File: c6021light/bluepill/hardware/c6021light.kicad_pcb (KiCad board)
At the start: 2 copper layers, 100 x 50 mm, 80 parts, among them J1 Barrel_Jack_Switch, J10 Conn_01x02, J11 Conn_01x02, J12 XpressNet, J2 Conn_02x04_Odd_Even, J3 Conn_02x16_Row_Letter_First, J30 Loconet, J31 Conn_01x02, J32 Conn_01x02, J4 Conn_01x02, J5 Grove I2C, J50 USB_B_Micro, J51 Conn_01x06, J52 Debug UART, J6 Conn_01x02, J7 Conn_01x02, J8 RJ45, Q30 BC337, Q31 BC547, Q32 BC547, SW1 SW_Push, U1 L7805, U10 SN75176, U2 L7808, U3 MCP2562, U30 LM393, U4 ISO1050DUB, U50 CH340C

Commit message: fix some bugs on PCb
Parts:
- moved C52 2.73 mm to (177.2, 60.9)
- moved D1 2.21 mm to (157.3, 57.0)
- moved J51 1.18 mm to (167.2, 64.1)
- moved C51 1.18 mm to (167.0, 54.9)
- moved U50 1.04 mm to (172.5, 60.6)
- moved C50 0.89 mm to (171.1, 54.0)
- moved R3 0.83 mm to (164.1, 64.2)
- moved R11 0.82 mm to (153.9, 60.8)
- moved R12 0.76 mm to (153.9, 63.8)
- moved J50 0.09 mm to (178.5, 52.8)
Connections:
- J51 pad 6: Net-(J51-Pad6) -> /RTS
- J52 pad 1: /DTR -> /CTS
- J52 pad 5: /CTS -> /RTS
- U50 pad 14: Net-(J51-Pad6) -> /RTS
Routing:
- net /DTR: track 17.7 -> 3.15 mm
- net /RTS: track 0.00 -> 10.4 mm
- net Net-(BP1-Pad25): track 19.1 -> 22.5 mm
- net /CTS: track 17.0 -> 20.0 mm
- net Net-(J51-Pad6): track 3.02 -> 0.00 mm
- net Net-(C52-Pad1): track 5.07 -> 2.33 mm
- net /TxD: track 68.2 -> 66.0 mm
- net Net-(BP1-Pad29): track 16.5 -> 18.3 mm
- net Net-(BP1-Pad30): track 12.8 -> 14.3 mm
- net Net-(D1-Pad2): track 3.13 -> 4.44 mm
- net GND: track 247.7 -> 246.5 mm, vias 24 -> 25
- net Net-(J50-Pad3): track 8.84 -> 9.92 mm, vias 2 -> 0
- net Net-(R12-Pad1): track 39.5 -> 40.6 mm
- net Net-(C50-Pad1): track 13.9 -> 13.3 mm
- net /RxD: track 72.3 -> 72.9 mm

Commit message: remove C32
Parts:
- removed C32: 1n, Capacitor_THT:C_Disc_D3.0mm_W1.6mm_P2.50mm
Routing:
- net Net-(C32-Pad1): track 29.0 -> 6.75 mm

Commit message: save PCB forgotten
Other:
- board text added: "Damian Philipp 2020/12 Gerhard Bertelsmann"
- board text removed: "Damian Philipp 2020/08 Gerhard Bertelsmann"

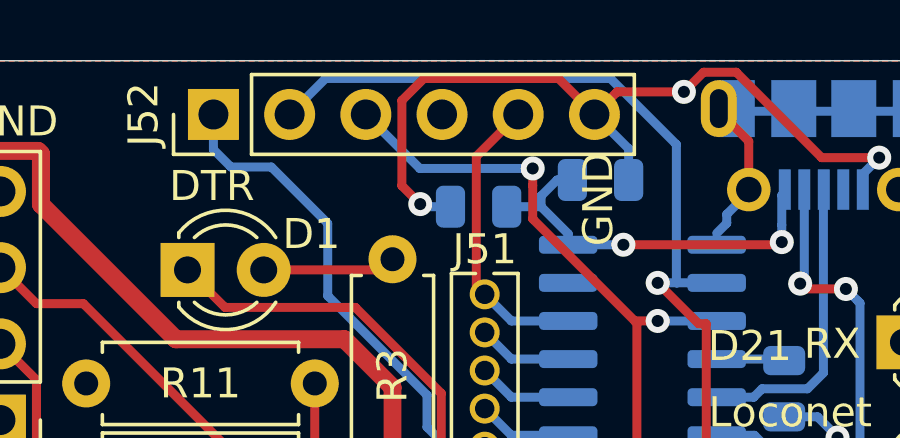
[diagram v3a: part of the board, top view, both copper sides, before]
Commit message: swap TxD and RxD on J52 header for standard USB2Serial Moduls
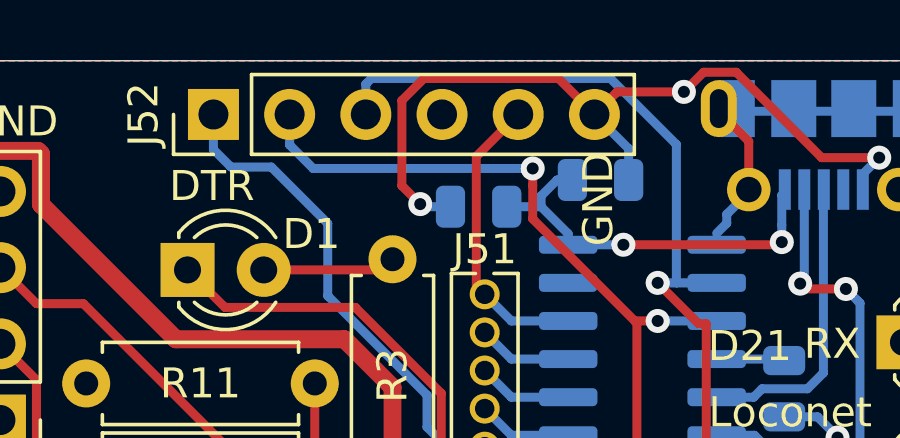
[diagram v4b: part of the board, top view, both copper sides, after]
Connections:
- J52 pad 2: /RxD -> /TxD
- J52 pad 3: /TxD -> /RxD
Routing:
- net /TxD: track 66.0 -> 69.1 mm
- net /RxD: track 72.9 -> 71.0 mm

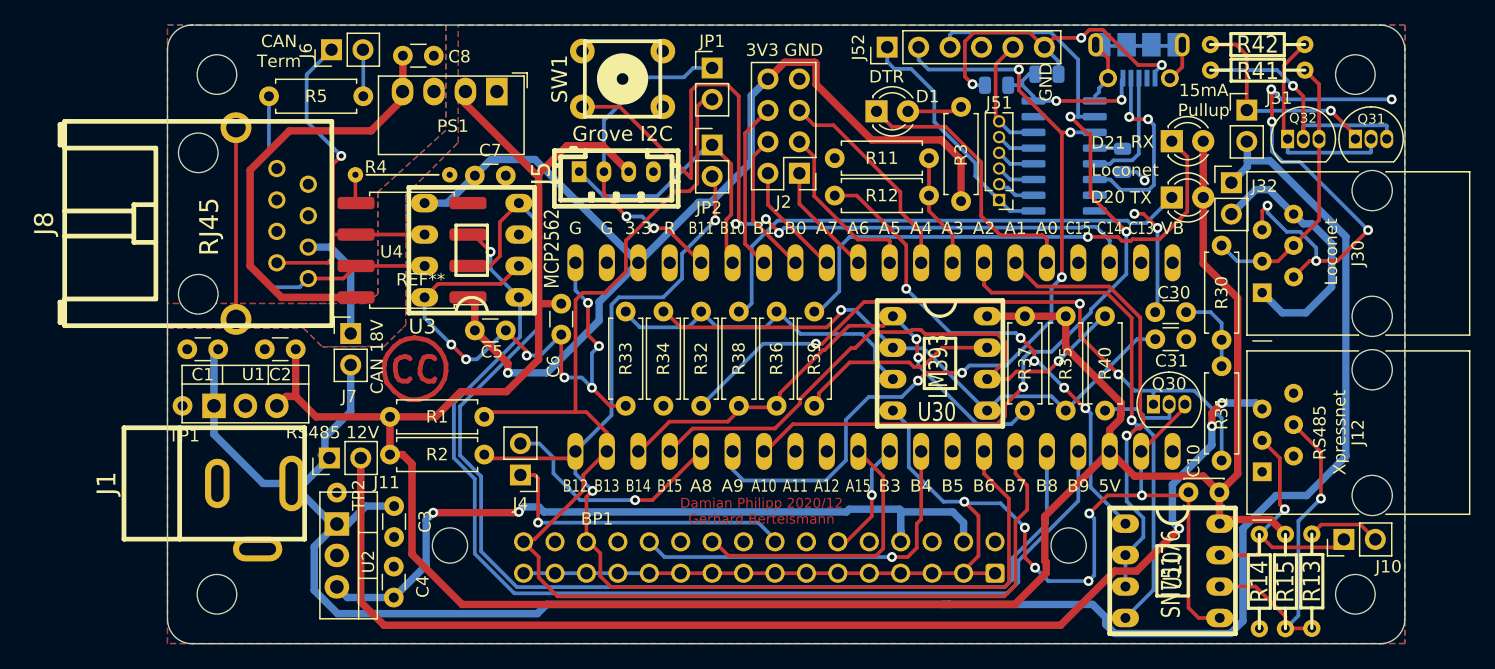
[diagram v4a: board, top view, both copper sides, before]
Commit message: fix silkscreen
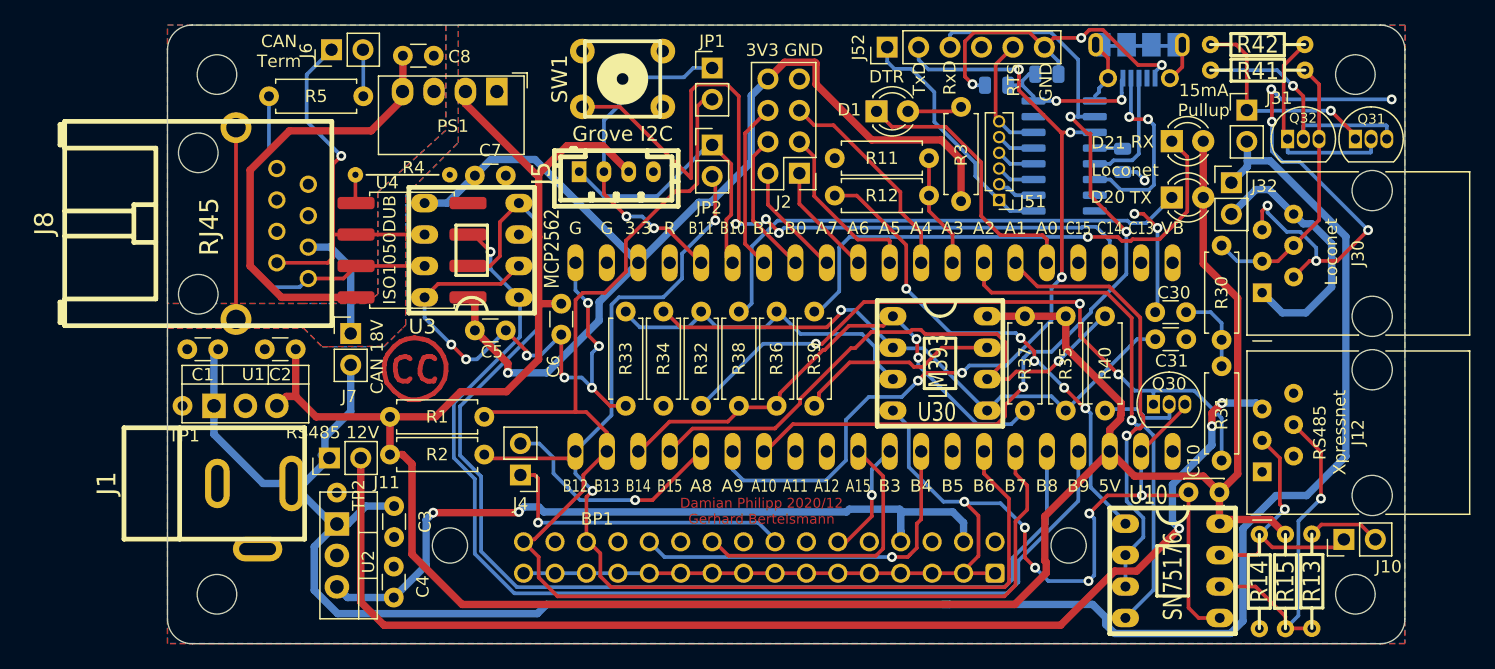
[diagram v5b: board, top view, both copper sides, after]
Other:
- board text added: "RTS"
- board text added: "RxD"
- board text added: "TxD"

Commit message: change PCB marking to 2021/01
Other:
- board text added: "Damian Philipp 2021/01 Gerhard Bertelsmann"
- board text removed: "Damian Philipp 2020/12 Gerhard Bertelsmann"
